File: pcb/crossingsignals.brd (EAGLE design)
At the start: 50.8 x 58.1 mm, 33 parts, among them J1 DETECT_4_SEND, J11 DEBUG, J2 DETECT_4_RCV, J3 DETECT_3_SEND, J4 DETECT_3_RCV, J5 DETECT_2_SEND, J6 DETECT_2_RCV, J7 DETECT_1_SEND, J8 DETECT_1_RCV, J9 POWER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

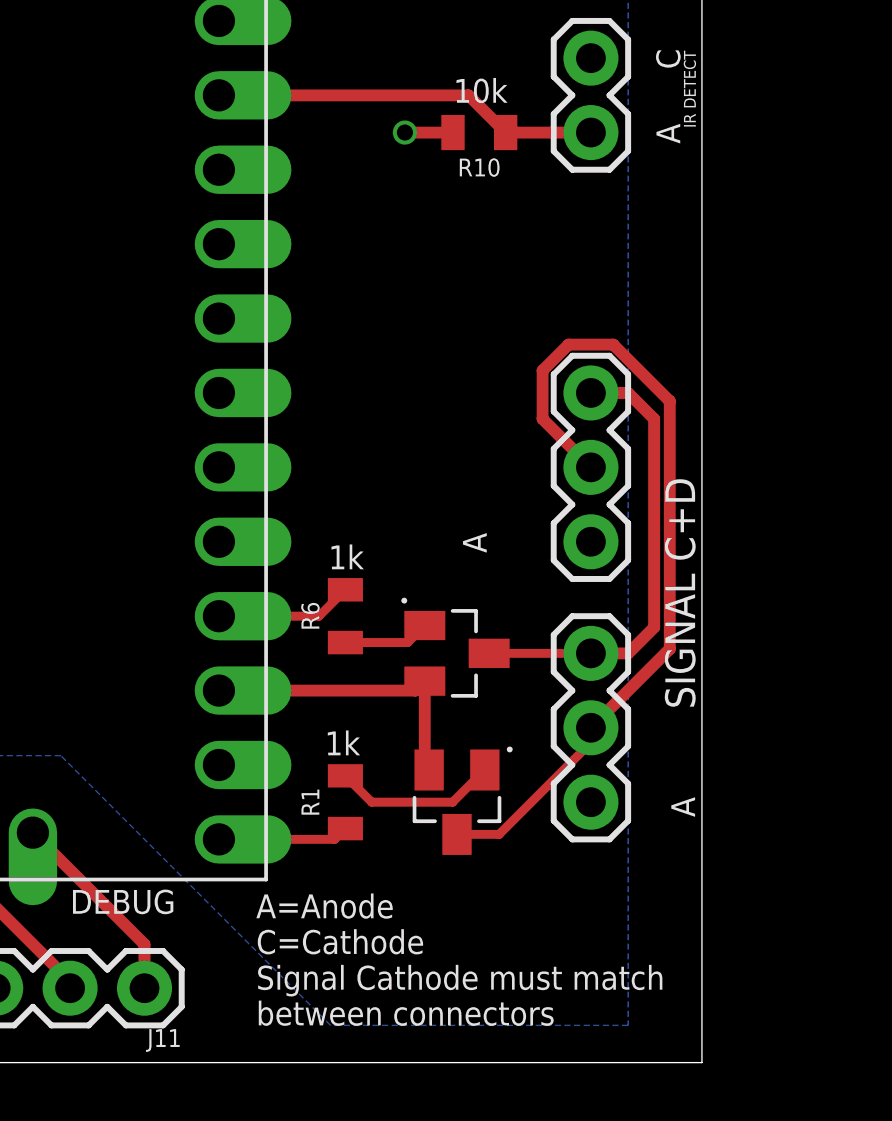
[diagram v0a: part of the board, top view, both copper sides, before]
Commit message: Adding a semaphore
* Add a GPIO signal to act as a semaphore in case anyone wants to know
when the signals are turned on or off
* Fix the handling of the interrupts. It's not individual functions and
should be smarter
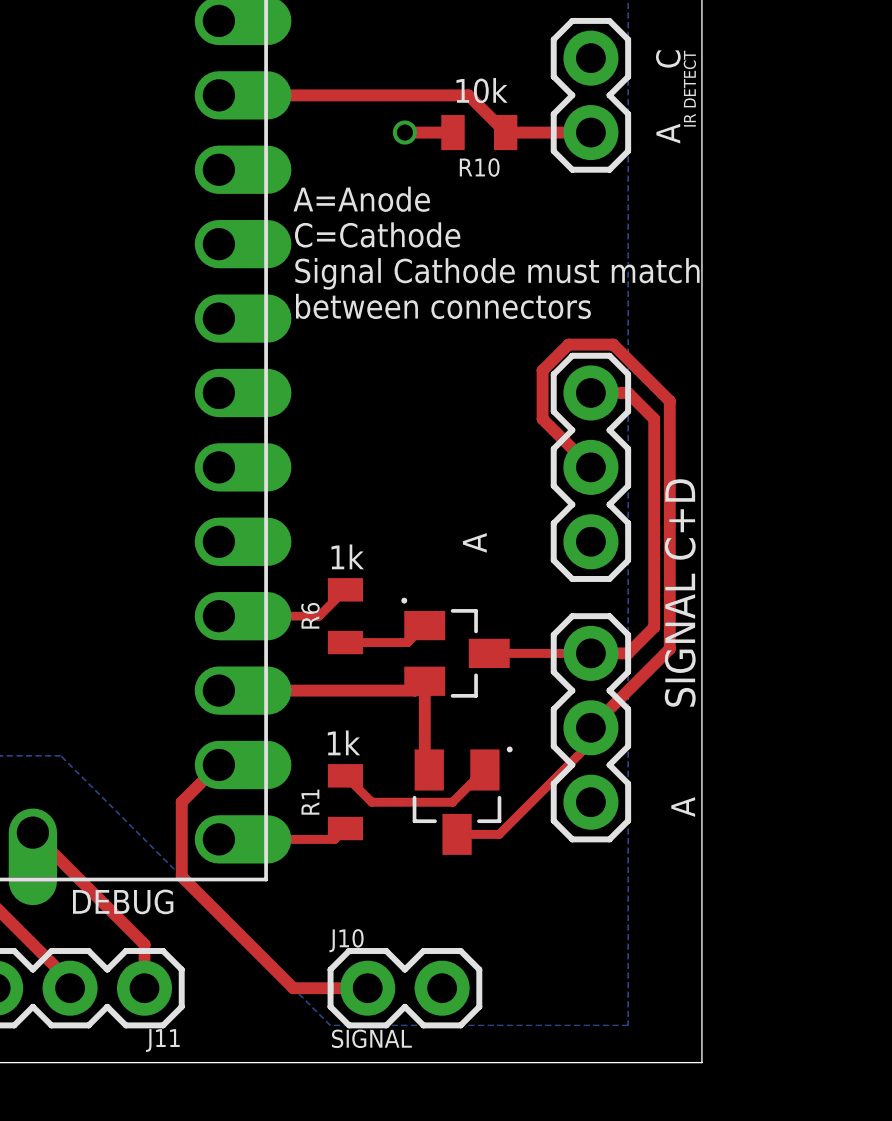
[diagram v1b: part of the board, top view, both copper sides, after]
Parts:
- added J10: SIGNAL, SparkFun-Connectors:1X02
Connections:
- new net GP17: J10.1, X1.GP17
- net GND: now also J10.2
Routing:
- net GP17: track 0.00 -> 12.3 mm
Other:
- board text added: "Crossing Signal Block (C) Peter Buelow February 2021 Version 1.1"
- board text removed: "Crossing Signal Block (C) Peter Buelow February 2021 Version 1.0"
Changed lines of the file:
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@@
 <text x="6.858" y="48.006" size="0.8128" layer="121">10k</text>
 <text x="42.418" y="48.006" size="0.8128" layer="121">10k</text>
-<text x="35.56" y="1.27" size="0.8128" layer="121">A=Anode
+<text x="36.83" y="25.4" size="0.8128" layer="121">A=Anode
 C=Cathode
 Signal Cathode must match
@@
 (C) Peter Buelow
 February 2021
-Version 1.0</text>
+Version 1.1</text>
 <text x="1.016" y="8.509" size="0.8128" layer="121" rot="R90">A</text>
 <text x="50.546" y="8.382" size="0.8128" layer="121" rot="R90">A</text>
@@
 <attribute name="VALUE" x="10.16" y="19.431" size="0.6096" layer="27" font="vector" ratio="20" align="top-center"/>
 </element>
+<element name="J10" library="SparkFun-Connectors" library_urn="urn:adsk.eagle:library:513" package="1X02" package3d_urn="urn:adsk.eagle:package:38039/1" value="SIGNAL" x="39.37" y="2.54" smashed="yes">
+<attribute name="NAME" x="38.1" y="3.937" size="0.6096" layer="25" font="vector" ratio="20"/>
+<attribute name="VALUE" x="38.1" y="0.508" size="0.6096" layer="121" font="vector" ratio="20"/>
+</element>
 </elements>
 <signals>
@@
 <contactref element="J9" pad="2"/>
 <contactref element="C1" pad="2"/>
+<contactref element="J10" pad="2"/>
 </signal>
 <signal name="OSDGND">
@@
 <wire x1="16.51" y1="2.54" x2="12.7" y2="2.54" width="1.27" layer="1"/>
 </signal>
+<signal name="GP17">
+<contactref element="J10" pad="1"/>
+<contactref element="X1" pad="GP17"/>
+<wire x1="34.29" y1="10.16" x2="33.02" y2="8.89" width="0.4064" layer="1"/>
+<wire x1="33.02" y1="8.89" x2="33.02" y2="6.35" width="0.4064" layer="1"/>
+<wire x1="33.02" y1="6.35" x2="36.83" y2="2.54" width="0.4064" layer="1"/>
+<wire x1="36.83" y1="2.54" x2="39.37" y2="2.54" width="0.4064" layer="1"/>
+</signal>
 </signals>
